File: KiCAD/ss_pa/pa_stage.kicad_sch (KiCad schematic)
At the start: 47 parts, among them J1 Conn_Coaxial_Small, J2 Screw_Terminal_01x02, J3 Conn_Coaxial_Small, J31 8P8C_Shielded, Q2 BS170, Q3 IRF510, Q4 IRF510, Q6 BS170, T201 BN61-2402, T202 BN61-2402, T203 T50-43, T204 BN43-202

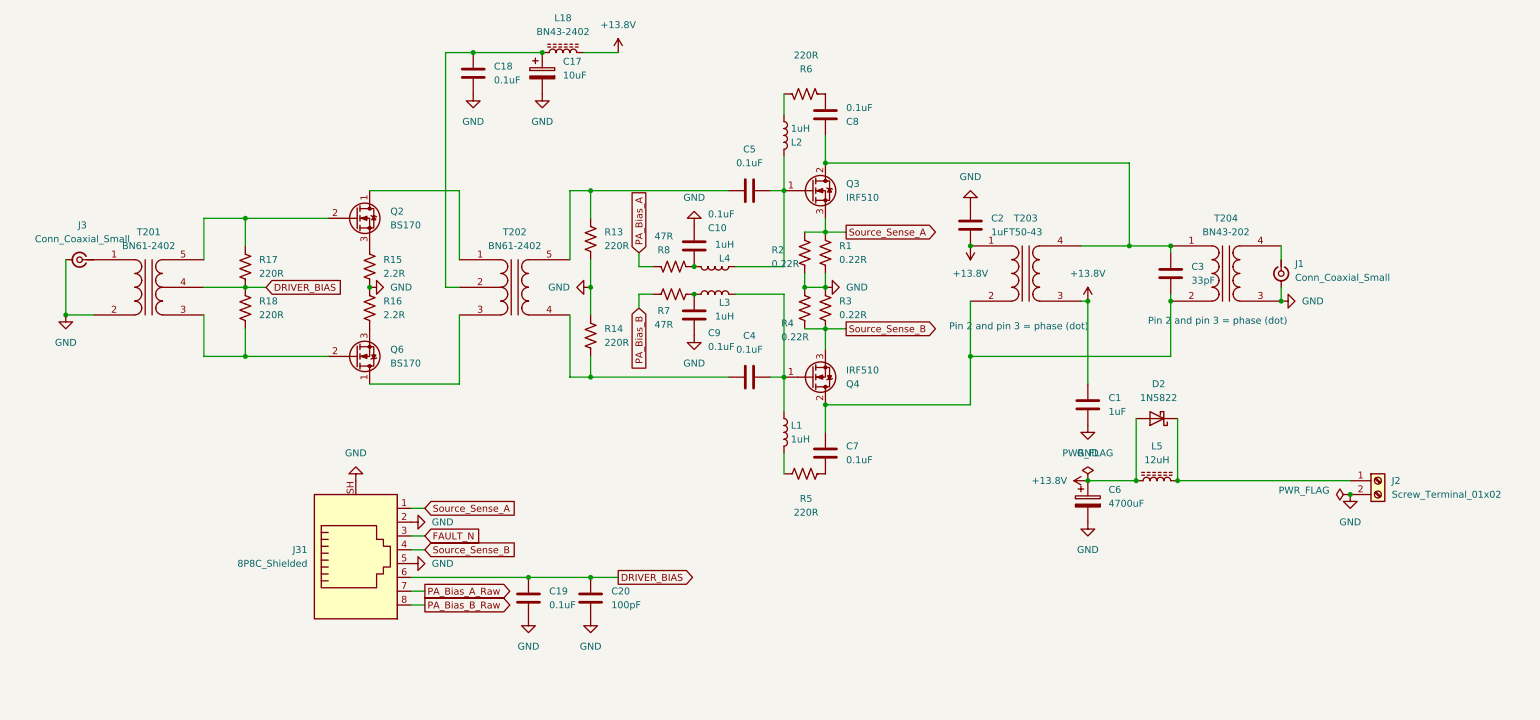
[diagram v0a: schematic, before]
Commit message: revD ss_pa: add test points (drains + RF out + bias + supply), 4-layer PCB
ss_pa test points added:
  TP1  +3.3V          - local U13 LDO output monitor
  TP2  PA_Bias_A      - IRF510 Q3 bias after fault switch (R12 pulldown)
  TP3  PA_Bias_B      - IRF510 Q4 bias after fault switch (R19 pulldown)
  TP4  (unconnected)  - orphan pad, clean up in next pass
  TP5  RF OUT         - J1 center pin, final 50 ohm matched RF out
  TP6  Q3 drain       - hot RF, oscillation check pad
  TP7  Q4 drain       - hot RF, oscillation check pad
  TP8  GND            - probe-return pad near one hot-RF TP
  TP9  GND            - probe-return pad near other hot-RF TP

Deliberately minimal set per earlier RF-stability discussion:
  * No TPs on BS170 drains, IRF510 gates, driver sources, or J3 RF
    input -- would require longer stubs that risk disturbing the
    VHF-tuned drain-gate feedback network. Mini-grabber on the
    device lead during bring-up is cleaner than a permanent pad.
  * Hot-RF TPs (TP5/6/7) are small-pad / short-stub.
  * Each hot-RF TP is paired with a nearby GND pad (TP8, TP9) so
    scope-probe ground spring reaches directly -- short probe loop
    for clean HF waveform, no antenna pickup.

4-layer PCB stackup planned for ss_pa (not 2-layer):
  * Outer layers: signal + GND pour
  * Inner layer 2: solid GND plane (uninterrupted)
  * Inner layer 3: solid +13.8 V plane (uninterrupted)
  * Via-stitching ties outer GND pours to inner GND plane
Benefits: cleaner RF return currents under driver + final chain,
lower-impedance power distribution for IRF510 pulse currents
(~2 A peak each), better heat spreading through +13.8 V plane
under the drain-feed region, reduced EMI radiation.

Docs updated:
  * Documentation/test_points.md -- added full ss_pa TP section
    with bring-up workflow (power-on sanity check, oscillation
    check, fault chain verification, RF level check). Doc title
    changed to cover both boards.
  * Documentation/Master_Description.md -- ss_pa section n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
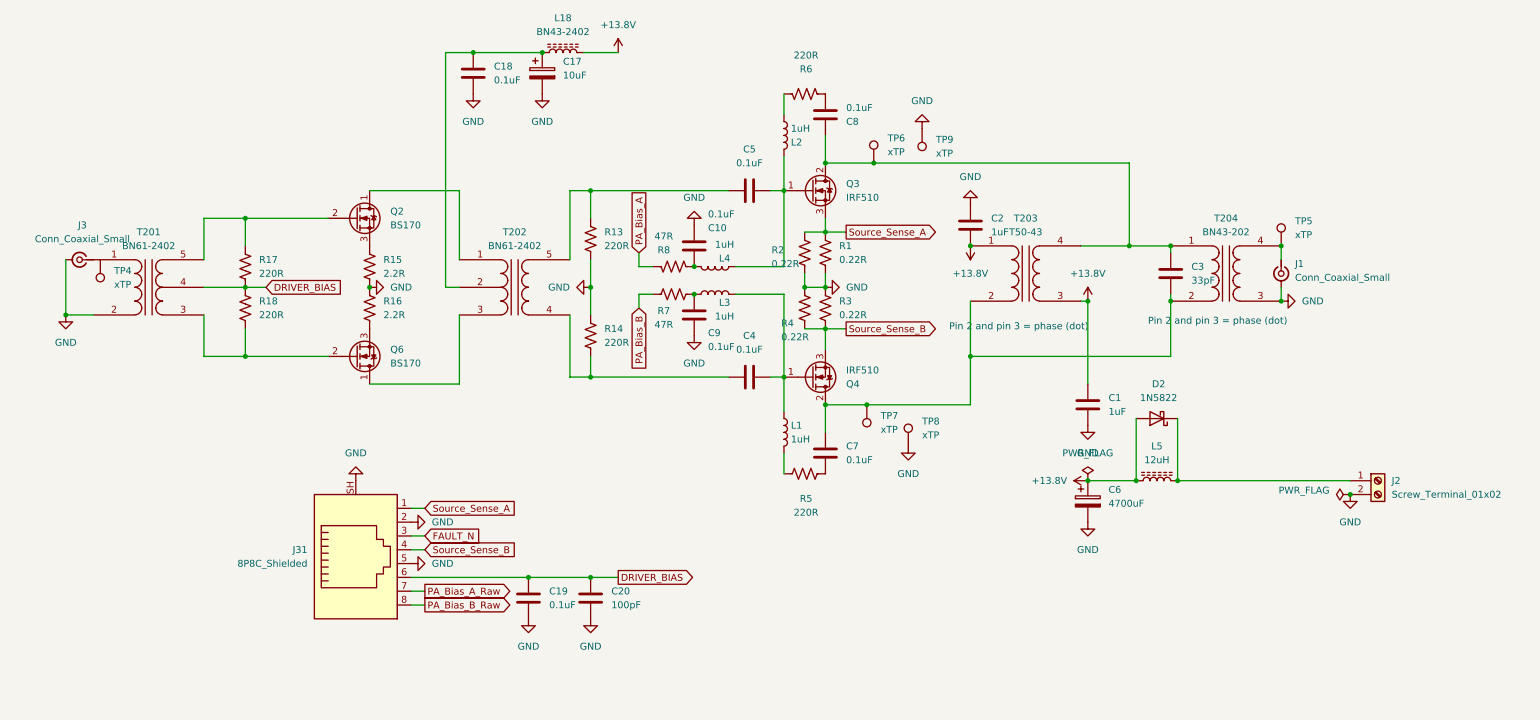
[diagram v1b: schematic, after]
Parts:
- added TP4, TP5, TP6, TP7, TP8, TP9: xTP, Connector_PinHeader_2.54mm:PinHeader_1x01_P2.54mm_Vertical, symbol xmitter:xTP
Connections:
- net GND: now also TP8.1, TP9.1
- net at C3.2, C7.2, Q4.2 (D)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: now also TP7.1
- net at J1.1 (In), T204.4 (SB): now also TP5.1
- net at C3.1, C8.2, Q3.2 (D)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: now also TP6.1

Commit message: revD ss_pa: fix L1-L4 footprint name (ERC), add two GND probe-return TPs
ERC fix:
  * L1, L2, L3, L4 (1 uH drain-gate feedback inductors) had
    footprint 'Inductor_THT:L_Axial_L5.3mm_D2.2mm_P2.54mm_Vertical'
    assigned, but the actual KiCad library footprint is named
    'L_Axial_L5.3mm_D2.2mm_P2.54mm_Vertical_Vishay_IM-1' (with the
    _Vishay_IM-1 suffix). Updated the schematic reference for all
    4 inductors to the correct name. KiCad can now resolve the
    footprint; next ERC run should show 0/0.

Test point additions on ss_pa:
  * TP10 GND -- probe-return pad near TP5 (RF OUT at J1)
  * TP11 GND -- probe-return pad near TP4 (RF IN at J3)

Combined with TP8 (near Q3 drain / TP6) and TP9 (near Q4 drain /
TP7), each hot-RF TP now has its own paired GND probe-return pad.
Short scope-probe-ground-spring loops at every RF measurement point.

Documentation/test_points.md updated with the clean 1:1 pairing:
  TP8  near TP6 (Q3 drain)
  TP9  near TP7 (Q4 drain)
  TP10 near TP5 (J1 RF out)
  TP11 near TP4 (J3 RF in)

Also updated tools/_assign_remaining_fp.py (gitignored scratch
script) with the correct footprint name so future re-runs don't
recreate the ERC warning.

ss_pa.kicad_pro: 4-layer PCB stackup selected per the earlier
discussion.

Co-Authored-By: Claude Opus 4.7 <noreply@anthropic.com>
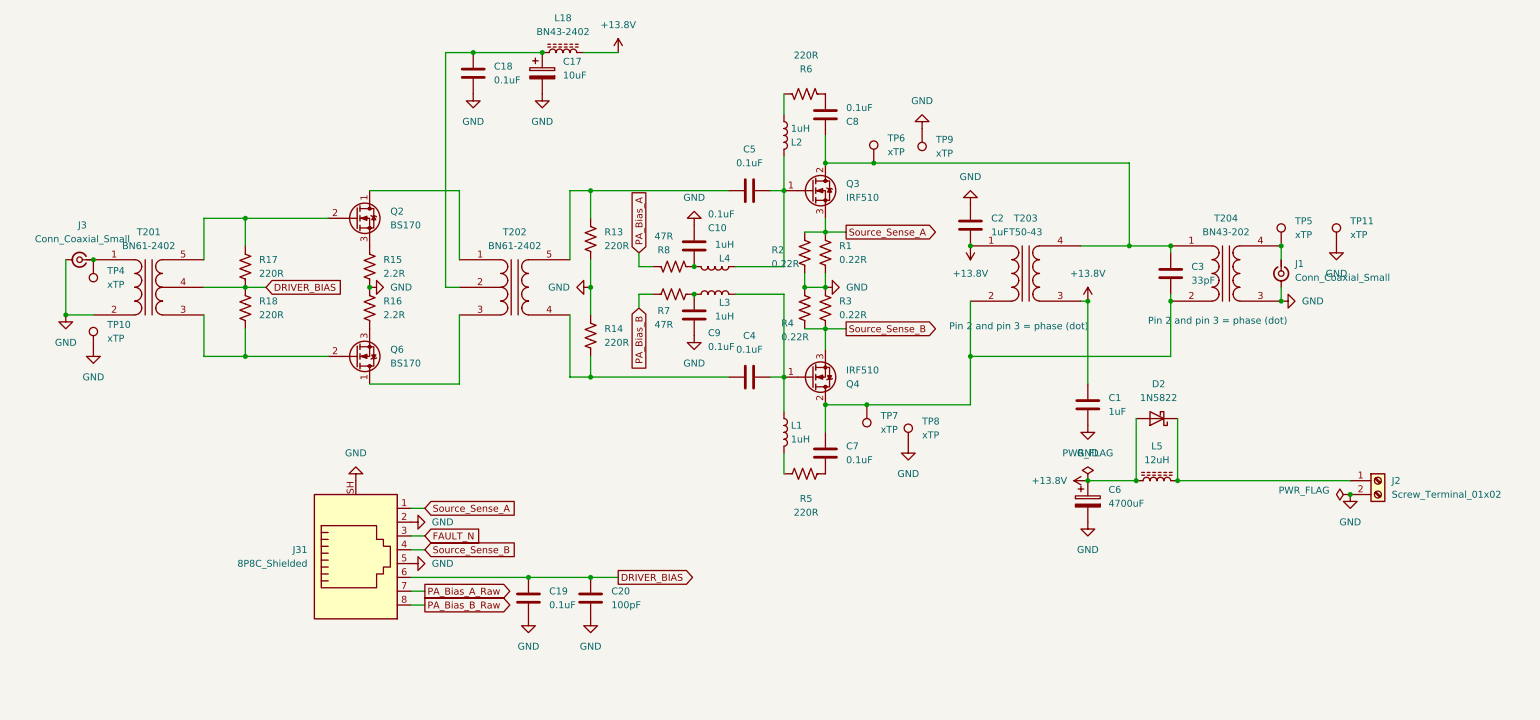
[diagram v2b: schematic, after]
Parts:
- added TP10, TP11: xTP, Connector_PinHeader_2.54mm:PinHeader_1x01_P2.54mm_Vertical, symbol xmitter:xTP
- L1, L2, L3, L4: footprint Inductor_THT:L_Axial_L5.3mm_D2.2mm_P2.54mm_Vertical -> Inductor_THT:L_Axial_L5.3mm_D2.2mm_P2.54mm_Vertical_Vishay_IM-1
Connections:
- net GND: now also TP10.1, TP11.1
- net at J3.1 (In), T201.1 (AA): now also TP4.1
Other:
- moved on the sheet: TP4

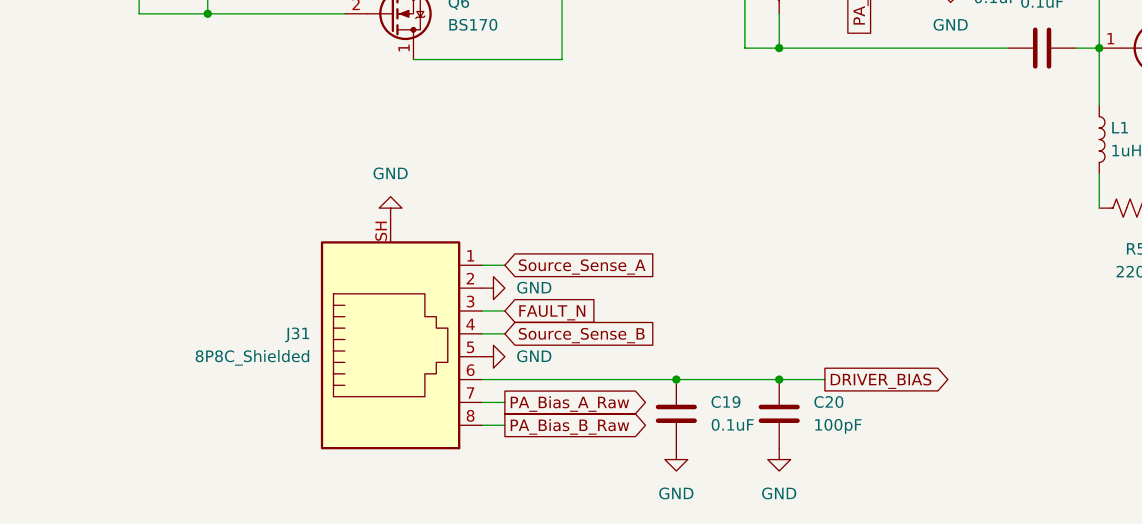
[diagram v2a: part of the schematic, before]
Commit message: revD: ss_pa Option C 5V rail + analog SW1 THT + R/C footprints + doc refresh
ss_pa Option C: swap U13 to LM2936Z-5.0 (full +5V logic rail), re-size
R10 10K->6.8K to preserve ~0.3V fault trip at new rail, drop +3.3V net
entirely. Fixes the previously-dead +5V bus that had no source.

Analog SW1 (Si5351 bringup DPDT): swap SMD footprint for
Button_Switch_THT:SW_CK_JS202011CQN_DPDT_Straight. Verified pin-numbering
convention (pin 1 above pin 6 in THT) matches user's intended DPST
wiring; both SDA/SCL break together.

Analog: assign missing footprints to R3/R4/R5/R8/R9 (DIN0207 axial) and
C4/C5/C6/C7/C8 (disc ceramic 5mm). Add xmitter:DIP-14_W7.62mm.kicad_mod
and 74HCT125 symbol to the xmitter library.

Documentation: Rev D handoff doc updated with M1-M8 fix status, Option C
notes, I2C bus voltage architecture, 74HCT125 SPI shifter, FAULT_N
divider details, and Metro-no-footprint note. Supporting docs updated:
i2c_bus.md full rewrite for 5V HV bus + STEMMA reroute, revD_interconnect
board inventory refresh, status banners on ss_pa.md / Master_Description /
cw_envelope_keyer / front_panel_interface pointing to handoff doc for
items beyond their last-current date.

Co-Authored-By: Claude Opus 4.7 <noreply@anthropic.com>
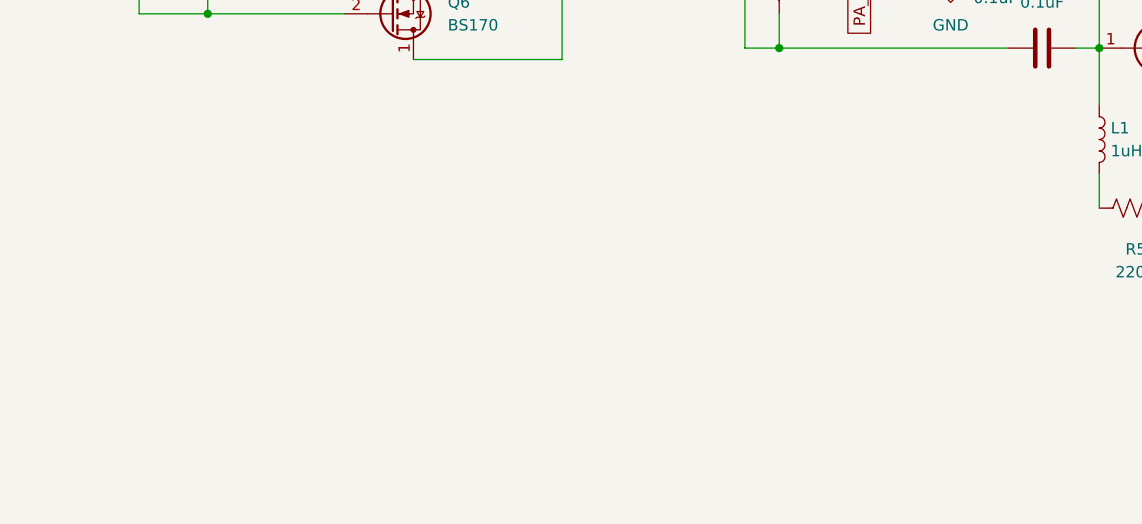
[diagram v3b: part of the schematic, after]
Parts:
- removed C19: 0.1uF, Capacitor_THT:C_Disc_D5.0mm_W2.5mm_P5.00mm, symbol Device:C
- removed C20: 100pF, Capacitor_THT:C_Rect_L7.0mm_W3.5mm_P5.00mm, symbol Device:C
- removed J31: 8P8C_Shielded, xmitter:Amphenol_RJE1D-188_Horizontal_Shielded, symbol Connector:8P8C_Shielded

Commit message: revD: analog + ss_pa RF filtering on umbilical signals
ss_pa: 1 uH RFC + bypass cap(s) added on each umbilical-crossing signal
to attenuate 14 MHz ingress from the cable and keep hot IRF510-source
RF from being injected back into the umbilical:

- PA_Bias_A_Raw: L6 1uH + C13 100nF + C26 100pF at J31.7
- PA_Bias_B_Raw: L7 1uH + C22 100nF + C27 100pF at J31.8
- Source_Sense_A: L8 1uH + C23 100nF between IRF510A source tap and
  the shared comparator/ADC node (new Source_Sense_A_Raw holds the
  Kelvin sense resistors R1/R2)
- Source_Sense_B: L9 1uH + C24 100nF, mirror of A on Q4 side
- DRIVER_BIAS: R20 100R + C19 0.1uF + C20 100pF already placed
  previously
- FAULT_N: R23 100R + C25 100pF filter on the external side of the
  latch (LM393 outputs + R9 pullup remain on the internal node for
  fast latching, R23 isolates from umbilical and 4066 enables)

Attenuation ~40-60 dB at 14 MHz across all five umbilical signals.

Analog: companion schematic touches for the DGFET G2 op-amp mute
subcircuit on the test sheet.

Co-Authored-By: Claude Opus 4.7 <noreply@anthropic.com>
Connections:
- net DRIVER_BIAS renamed DRIVER_BIAS_CLEAN
- net Source_Sense_A renamed Source_Sense_A_Raw
- net Source_Sense_B renamed Source_Sense_B_Raw
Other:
- moved on the sheet: J3, R17, R18, T201, TP10, TP4

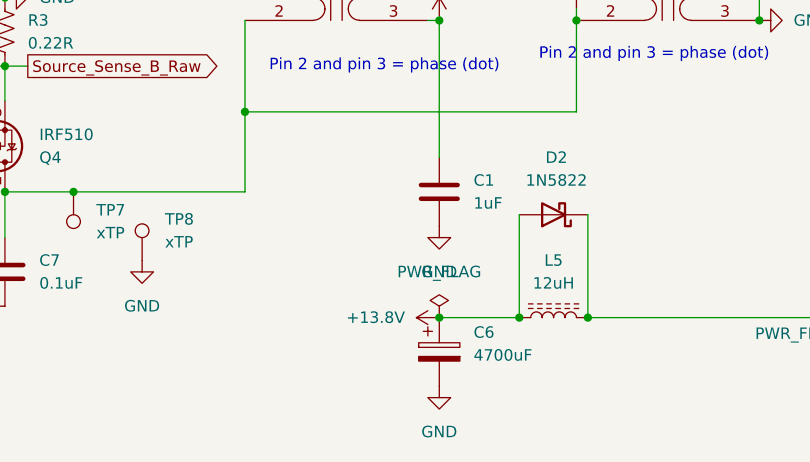
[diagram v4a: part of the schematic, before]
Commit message: revD: ss_pa U13 LM2936 pinout fix + analog U9 74HCT125 miswiring fix
ss_pa fault_shutdown.kicad_sch: fix U13 pin-to-signal mapping so an
LM2936Z-5.0/NOPB can be installed without destruction (prior MCP1700
symbol had pin 1=GND, 2=VI, 3=VO; LM2936 datasheet is pin 1=VO, 2=GND,
3=VI).

analog dac.kicad_sch: fix U9 74HCT125 miswiring found during follow-up
audit.

Co-Authored-By: Claude Opus 4.7 <noreply@anthropic.com>
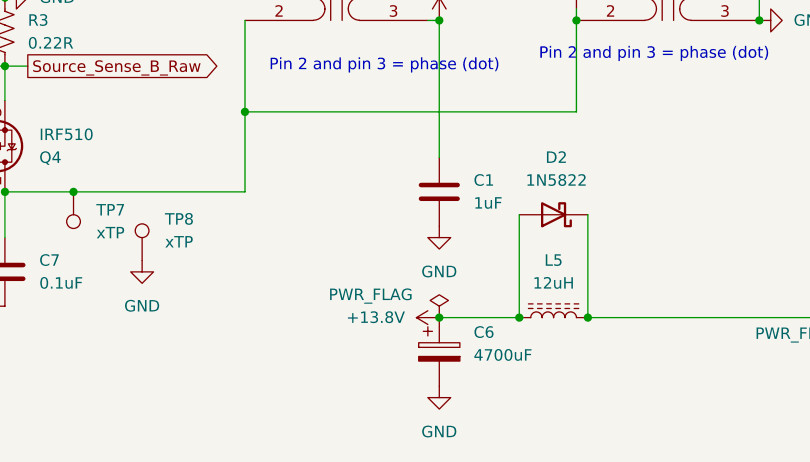
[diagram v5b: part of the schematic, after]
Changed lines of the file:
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@@
 		(in_pos_files yes)
 		(dnp no)
-		(fields_autoplaced yes)
 		(property "Reference" "#FLG01"
 			(at 209.55 126.365 0)
@@
 		)
 		(property "Value" "PWR_FLAG"
-			(at 209.55 123.19 0)
+			(at 201.93 125.73 0)
 			(show_name no)
 			(do_not_autoplace no)
